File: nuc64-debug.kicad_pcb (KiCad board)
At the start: 2 copper layers, 21.6 x 18.4 mm, 5 parts

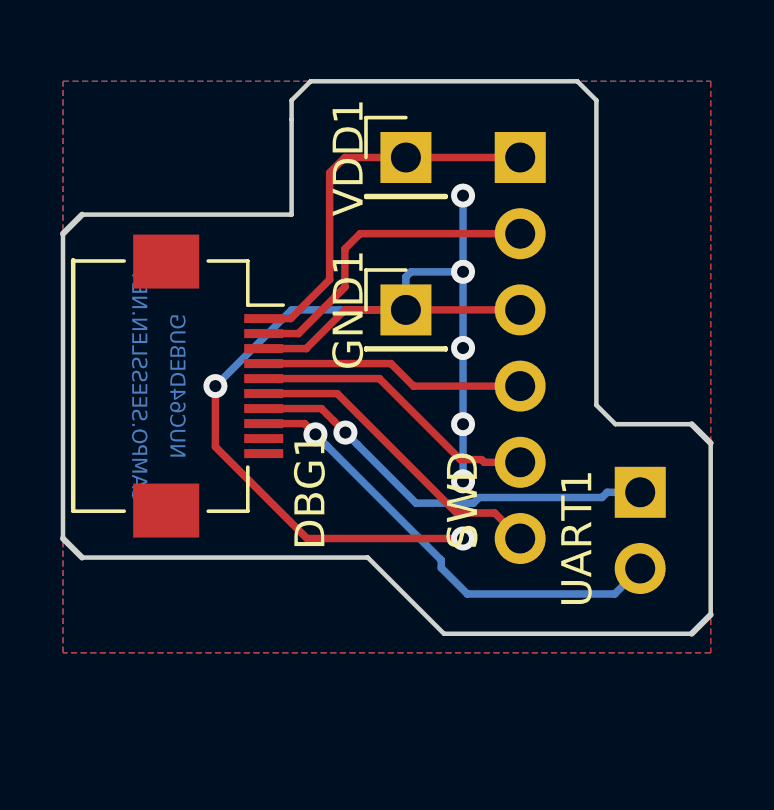
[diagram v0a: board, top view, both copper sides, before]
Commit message: added some grounding vias
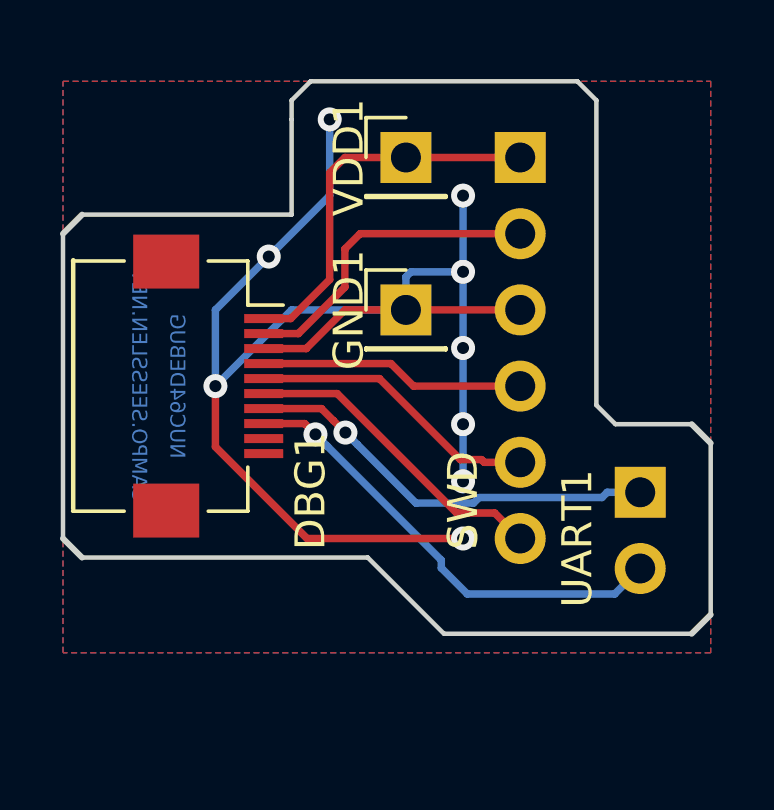
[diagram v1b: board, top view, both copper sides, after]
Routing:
- net GND: track 40.6 -> 51.1 mm, vias 7 -> 9
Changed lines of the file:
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@@
     (thickness 1.6)
     (drawings 20)
-    (tracks 66)
+    (tracks 72)
     (zones 0)
     (modules 5)
@@
   (via (at 117.475 83.82) (size 0.8) (drill 0.4) (layers F.Cu B.Cu) (net 8))
   (segment (start 112.274998 83.82) (end 117.475 83.82) (width 0.25) (layer F.Cu) (net 8))
+  (via (at 110.998 74.422) (size 0.8) (drill 0.4) (layers F.Cu B.Cu) (net 8))
+  (segment (start 109.22 78.74) (end 109.22 76.2) (width 0.25) (layer B.Cu) (net 8))
+  (segment (start 109.22 76.2) (end 110.998 74.422) (width 0.25) (layer B.Cu) (net 8))
+  (via (at 113.03 69.85) (size 0.8) (drill 0.4) (layers F.Cu B.Cu) (net 8))
+  (segment (start 110.998 74.422) (end 113.03 72.39) (width 0.25) (layer B.Cu) (net 8))
+  (segment (start 113.03 72.39) (end 113.03 69.85) (width 0.25) (layer B.Cu) (net 8))
   (zone (net 8) (net_name GND) (layer F.Cu) (hatch edge 0.508)
     (connect_pads (clearance 0.508))

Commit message: fixed drawings
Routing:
- net GND: track 51.1 -> 48.6 mm
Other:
- board text added: "V0.1"
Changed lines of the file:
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@@
   (general
     (thickness 1.6)
-    (drawings 20)
+    (drawings 23)
     (tracks 72)
     (zones 0)
@@
       (rotate (xyz 0 0 0))
     )
+  )
+  (gr_text V0.1 (at 112.522 76.962 270) (layer B.Cu)
+    (effects (font (size 0.5 0.5) (thickness 0.125)) (justify mirror))
+  )
+  (dimension 4.064 (width 0.3) (layer Dwgs.User)
+    (gr_text "4,064 mm" (at 121.412 91) (layer Dwgs.User)
+      (effects (font (size 1.5 1.5) (thickness 0.3)))
+    )
+    (feature1 (pts (xy 123.444 83.82) (xy 123.444 89.486421)))
+    (feature2 (pts (xy 119.38 83.82) (xy 119.38 89.486421)))
+    (crossbar (pts (xy 119.38 88.9) (xy 123.444 88.9)))
+    (arrow1a (pts (xy 123.444 88.9) (xy 122.317496 89.486421)))
+    (arrow1b (pts (xy 123.444 88.9) (xy 122.317496 88.313579)))
+    (arrow2a (pts (xy 119.38 88.9) (xy 120.506504 89.486421)))
+    (arrow2b (pts (xy 119.38 88.9) (xy 120.506504 88.313579)))
+  )
+  (dimension 1.016 (width 0.3) (layer Dwgs.User)
+    (gr_text "1,016 mm" (at 129.608 81.788 90) (layer Dwgs.User)
+      (effects (font (size 1.5 1.5) (thickness 0.3)))
+    )
+    (feature1 (pts (xy 123.444 81.28) (xy 128.094421 81.28)))
+    (feature2 (pts (xy 123.444 82.296) (xy 128.094421 82.296)))
+    (crossbar (pts (xy 127.508 82.296) (xy 127.508 81.28)))
+    (arrow1a (pts (xy 127.508 81.28) (xy 128.094421 82.406504)))
+    (arrow1b (pts (xy 127.508 81.28) (xy 126.921579 82.406504)))
+    (arrow2a (pts (xy 127.508 82.296) (xy 128.094421 81.169496)))
+    (arrow2b (pts (xy 127.508 82.296) (xy 126.921579 81.169496)))
   )
   (gr_line (start 122.555 80.01) (end 121.92 79.375) (layer Edge.Cuts) (width 0.15))
@@
   (segment (start 115.57 76.2) (end 119.38 76.2) (width 0.25) (layer F.Cu) (net 8) (status 30))
   (via (at 109.22 78.74) (size 0.8) (drill 0.4) (layers F.Cu B.Cu) (net 8))
-  (segment (start 115.57 76.2) (end 111.76 76.2) (width 0.25) (layer B.Cu) (net 8))
-  (segment (start 111.76 76.2) (end 109.22 78.74) (width 0.25) (layer B.Cu) (net 8))
   (via (at 117.475 74.93) (size 0.8) (drill 0.4) (layers F.Cu B.Cu) (net 8))
   (segment (start 115.74 74.93) (end 117.475 74.93) (width 0.25) (layer B.Cu) (net 8))
-  (segment (start 115.57 76.2) (end 115.57 75.1) (width 0.25) (layer B.Cu) (net 8))
   (segment (start 115.57 75.1) (end 115.74 74.93) (width 0.25) (layer B.Cu) (net 8))
   (via (at 117.475 72.39) (size 0.8) (drill 0.4) (layers F.Cu B.Cu) (net 8))
@@
   (segment (start 110.998 74.422) (end 113.03 72.39) (width 0.25) (layer B.Cu) (net 8))
   (segment (start 113.03 72.39) (end 113.03 69.85) (width 0.25) (layer B.Cu) (net 8))
+  (segment (start 115.57 75.1) (end 115.57 76.2) (width 0.25) (layer B.Cu) (net 8))
+  (segment (start 114.892 74.422) (end 115.57 75.1) (width 0.25) (layer B.Cu) (net 8))
+  (segment (start 110.998 74.422) (end 114.892 74.422) (width 0.25) (layer B.Cu) (net 8))
   (zone (net 8) (net_name GND) (layer F.Cu) (hatch edge 0.508)
     (connect_pads (clearance 0.508))

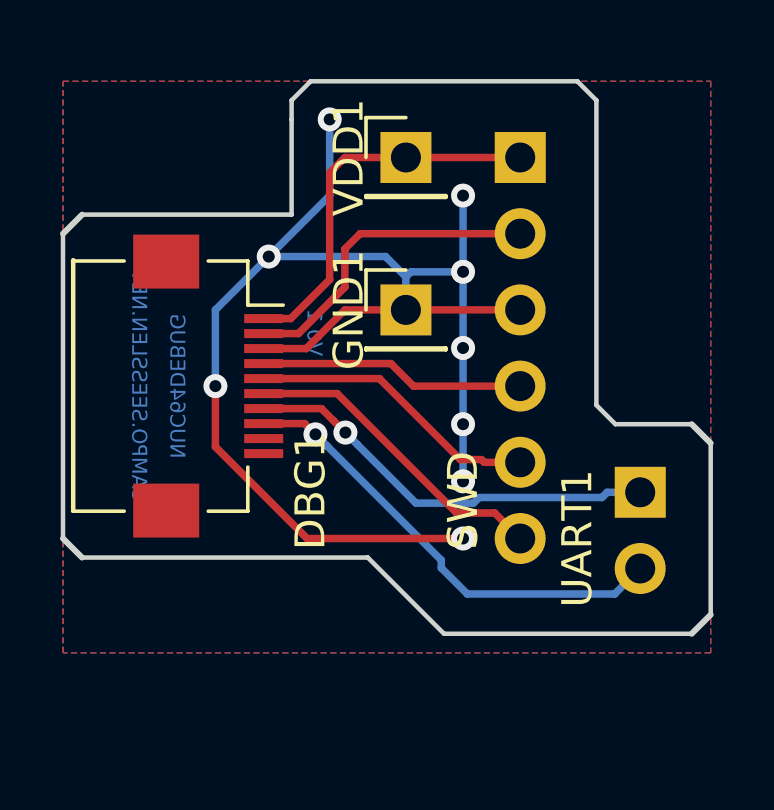
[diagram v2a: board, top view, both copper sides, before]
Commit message: First draft for 0.2.x
Uart TX/RX have been swapped
Buttons for Reset/Boot0 have been added
Pinheader for power pins has been added
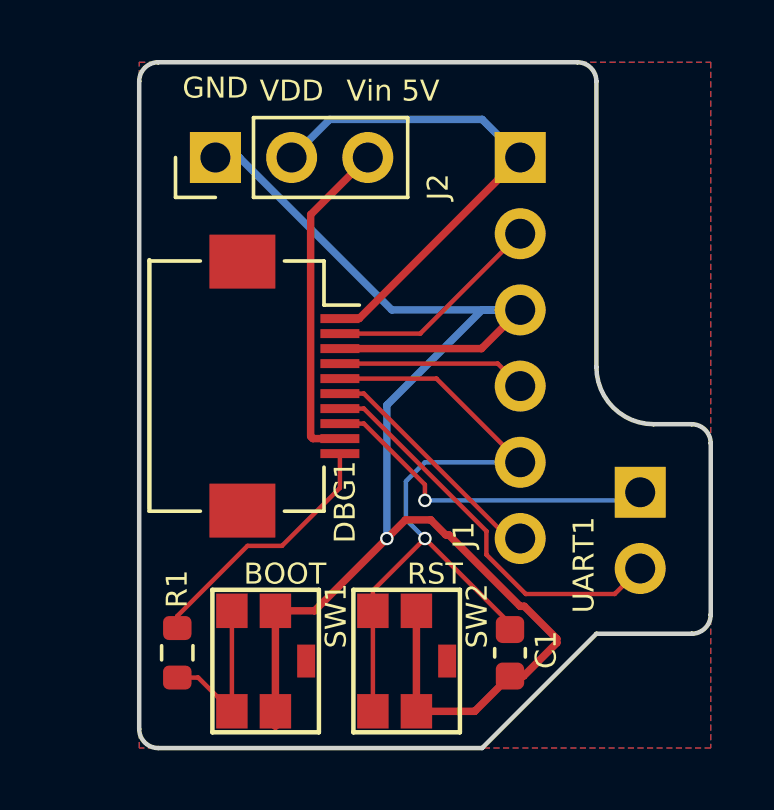
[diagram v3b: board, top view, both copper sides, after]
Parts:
- removed GND1, VDD1: Conn_01x01_Male, Connector_PinHeader_2.54mm:PinHeader_1x01_P2.54mm_Vertical
- added C1: 100n, Capacitor_SMD:C_0603_1608Metric, F.Cu at (119.0, 87.6)
- added J2: POW, Connector_PinHeader_2.54mm:PinHeader_1x03_P2.54mm_Vertical, F.Cu at (109.2, 71.1)
- added R1: 330, Resistor_SMD:R_0603_1608Metric, F.Cu at (108.0, 87.6)
- added SW1: BOOT, footprints:panasonic_evpa302k, F.Cu at (110.5, 87.9)
- added SW2: RST, footprints:panasonic_evpa302k, F.Cu at (115.2, 87.9)
- DBG1: value Conn_01x10_Female -> DBG
- UART1: value Conn_01x02_Male -> UART
- moved DBG1 2.54 mm to (109.2, 78.7)
- renumbered SWD to J1
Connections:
- DBG1 pad 10: (no net) -> Net-(DBG1-Pad10)
- DBG1 pad 9: (no net) -> Net-(DBG1-Pad9)
- UART1 pad 1: Net-(DBG1-Pad7) -> Net-(DBG1-Pad8)
- UART1 pad 2: Net-(DBG1-Pad8) -> Net-(DBG1-Pad7)
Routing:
- net /NRST: track 9.71 -> 24.1 mm, vias 0 -> 1
- net Net-(DBG1-Pad9): track 0.00 -> 11.1 mm
- net Net-(DBG1-Pad10): track 0.00 -> 8.73 mm
- net GND: track 48.6 -> 54.7 mm, vias 9 -> 1
- net Net-(R1-Pad2): track 0.00 -> 5.64 mm
- net /VDD: track 12.9 -> 16.9 mm
- net Net-(DBG1-Pad8): track 15.4 -> 11.5 mm
- net /SWCLK: track 10.7 -> 7.39 mm
- net /SWO: track 10.6 -> 8.01 mm
- net /SWDIO: track 8.86 -> 6.32 mm
- net Net-(DBG1-Pad7): track 14.0 -> 13.4 mm, vias 1 -> 0
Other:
- board size 21.6 x 18.4 mm -> 19.1 x 22.9 mm
- net class Default: trace_width 0.25 -> 0.15; via_dia 0.8 -> 0.45; via_drill 0.4 -> 0.3
- net class power added: clearance 0.2, trace_width 0.25, via_dia 0.45, via_drill 0.3
- rule trace_min: 0.2 -> 0.15
- board text added: "GND"
- board text added: "NUC64DEBUG V0.2.x 20210714"
- board text added: "VDD"
- board text added: "Vin 5V"
- board text removed: "NUC64DEBUG"
- board text removed: "V0.1"

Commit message: shrink
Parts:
- added D1: LED, LED_SMD:LED_0603_1608Metric, F.Cu at (122.1, 71.9)
- added R2: R, Resistor_SMD:R_0603_1608Metric, F.Cu at (122.1, 75.1)
- moved DBG1 2.54 mm to (111.8, 78.7)
- moved R1 1.95 mm to (109.9, 87.7)
- moved SW1 1.80 mm to (112.3, 87.9)
- moved J2 1.27 mm to (110.5, 71.1)
- moved SW2 1.11 mm to (116.3, 87.9)
- moved C1 0.84 mm to (119.6, 87.0)
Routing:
- net GND: track 54.7 -> 52.0 mm
- net /SWDIO: track 6.32 -> 3.78 mm
- net /SWCLK: track 7.39 -> 5.24 mm
- net Net-(D1-Pad1): track 0.00 -> 1.79 mm
- net Net-(DBG1-Pad7): track 13.4 -> 11.7 mm
- net Net-(DBG1-Pad9): track 11.1 -> 12.6 mm
- net Net-(R1-Pad2): track 5.64 -> 7.05 mm
- net /NRST: track 24.1 -> 22.7 mm
- net Net-(DBG1-Pad8): track 11.5 -> 10.3 mm
- net Net-(DBG1-Pad10): track 8.73 -> 9.79 mm
- net /SWO: track 8.01 -> 7.12 mm
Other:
- board size 19.1 x 22.9 mm -> 17.1 x 22.9 mm
- board text added: "CAMPO.SEESSLEN.NET NUC64DEBUG V0.2.x 20210714"
- board text removed: "CAMPO.SEESSLEN.NET"
- board text removed: "NUC64DEBUG V0.2.x 20210714"
